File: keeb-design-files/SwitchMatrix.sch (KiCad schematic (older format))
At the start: 136 parts, among them SW10 8, SW11 9, SW12 0, SW13 -, SW14 =, SW15 BACKSPACE, SW16 HOME, SW17 TAB, SW18 CAPS LOCK, SW19 L_SHIFT, SW2 `, SW20 L_CTRL, SW21 Q, SW22 A, SW23 Z, SW24 WIN, SW25 W, SW26 S, SW27 X, SW28 L_ALT, SW29 E, SW3 1, SW30 D, SW31 C, SW32 SPACE, SW33 R, SW34 F, SW35 V, SW36 R_ALT, SW37 T, SW38 G, SW39 B, SW4 2, SW40 FN, SW41 Y, SW42 H, SW43 N, SW44 R_CTRL, SW45 U, SW46 J, SW47 M, SW48 LEFT, SW49 I, SW5 3, SW50 K, SW51 ,, SW52 DOWN, SW53 O, SW54 L, SW55 ., SW56 RIGHT, SW57 P, SW58 ;, SW59 /, SW6 4, SW60 [, SW61 ', SW62 R_SHIFT, SW63 ], SW64 ENTER, SW65 UP, SW66 \\, SW67 PAGE DOWN, SW68 END, SW69 PAGE UP, SW7 5, SW8 6, SW9 7

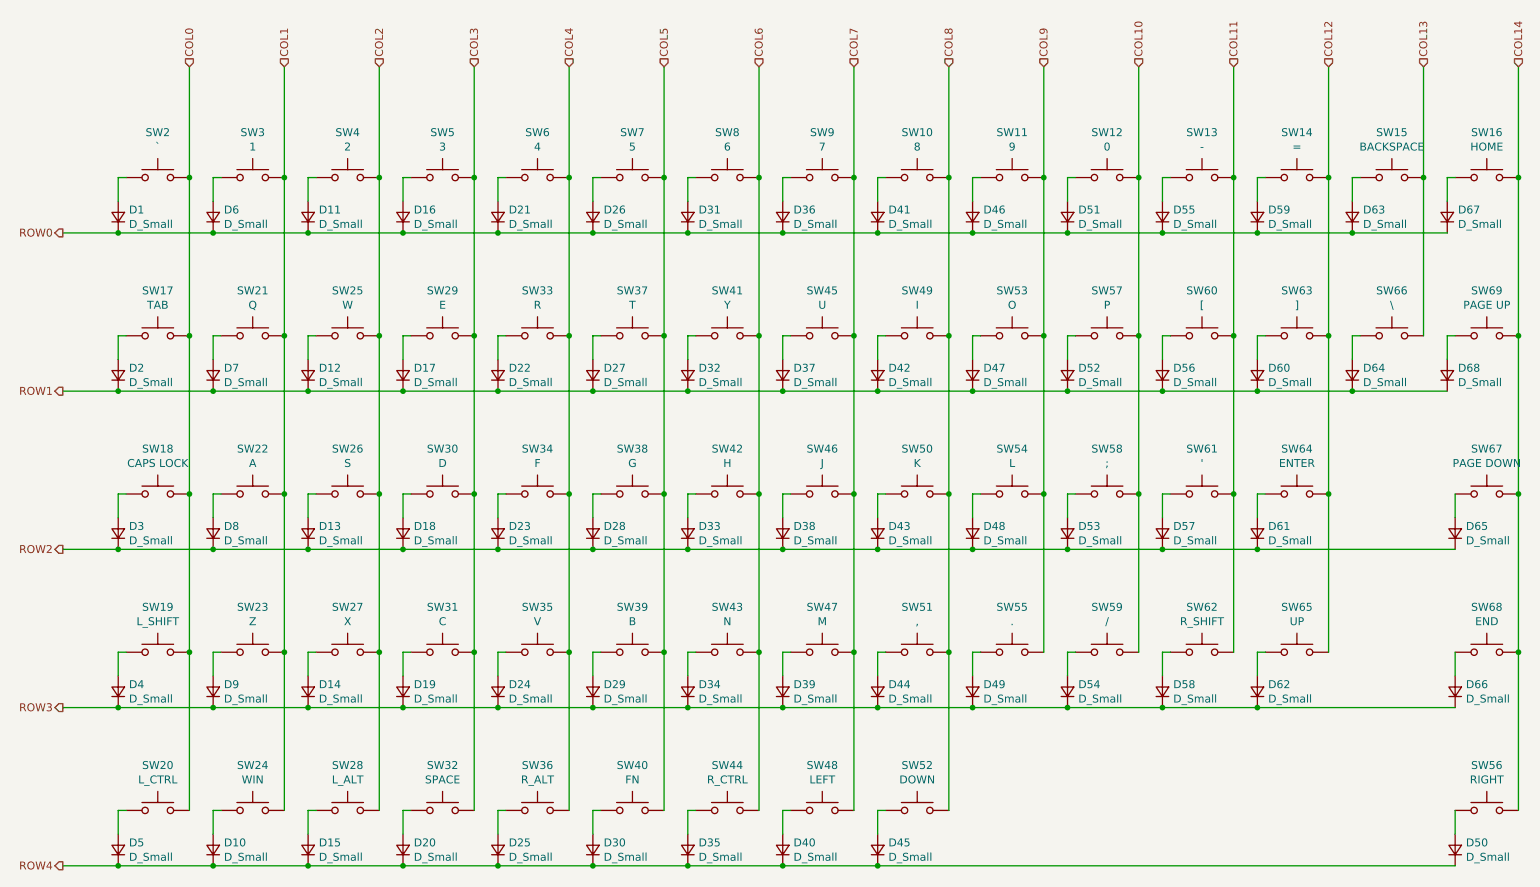
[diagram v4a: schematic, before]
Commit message: More routing added planes and re-wired MCU a bit
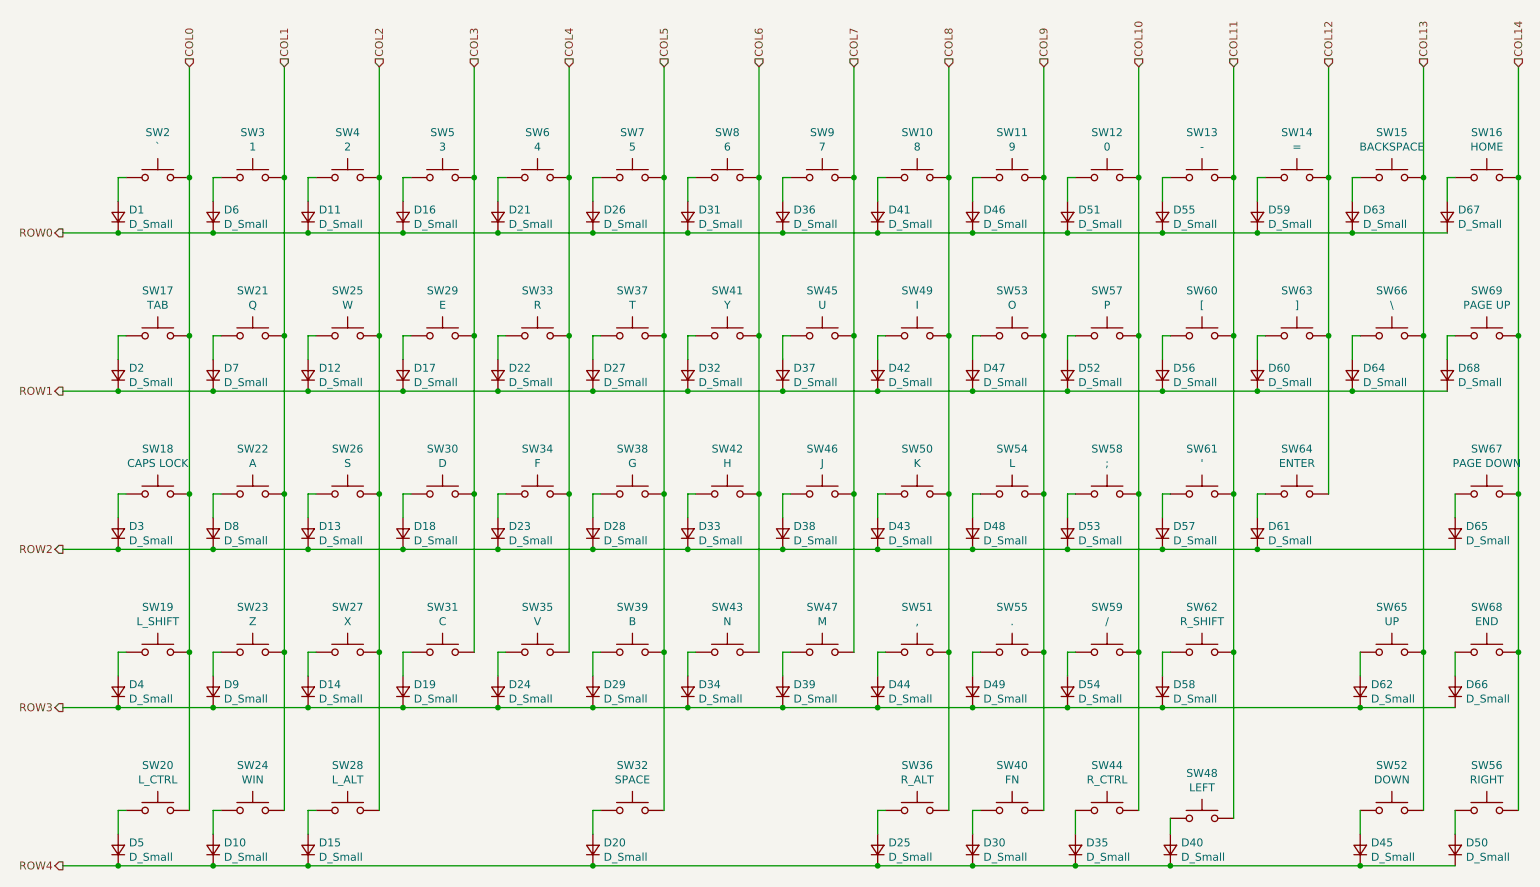
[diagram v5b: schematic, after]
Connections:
- net COL10: now also SW44.2
- net COL11: now also SW48.2
- net COL12: no longer SW65.2
- net COL13: now also SW52.2, SW65.2
- net COL3: no longer SW32.2
- net COL4: no longer SW36.2
- net COL5: now also SW32.2; no longer SW40.2
- net COL6: no longer SW44.2
- net COL7: no longer SW48.2
- net COL8: now also SW36.2; no longer SW52.2
- net COL9: now also SW40.2
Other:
- moved on the sheet: D20, D25, D30, D35, D40, D45, D62, SW32, SW36, SW40, SW44, SW48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

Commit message: Create gerbers picknplace and bom
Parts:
- D1, D10, D11, D12, D13, D14, D15, D16, D17, D18, D19, D2, D20, D21, D22, D23, D24, D25, D26, D27, D28, D29, D3, D30, D31, D32, D33, D34, D35, D36, D37, D38, D39, D4, D40, D41, D42, D43, D44, D45, D46, D47, D48, D49, D5, D50, D51, D52, D53, D54, D55, D56, D57, D58, D59, D6, D60, D61, D62, D63, D64, D65, D66, D67, D68, D7, D8, D9: LCSC Part Number C151442 -> C2128
